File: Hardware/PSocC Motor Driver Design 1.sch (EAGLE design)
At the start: 43 parts, among them J1 DNP, J2 DNP, J3 DNP, J4 DNP, J5 DNP, J6 DNP, J7 DNP, U1 CY8C4245LQI-483, U2 DRV8835

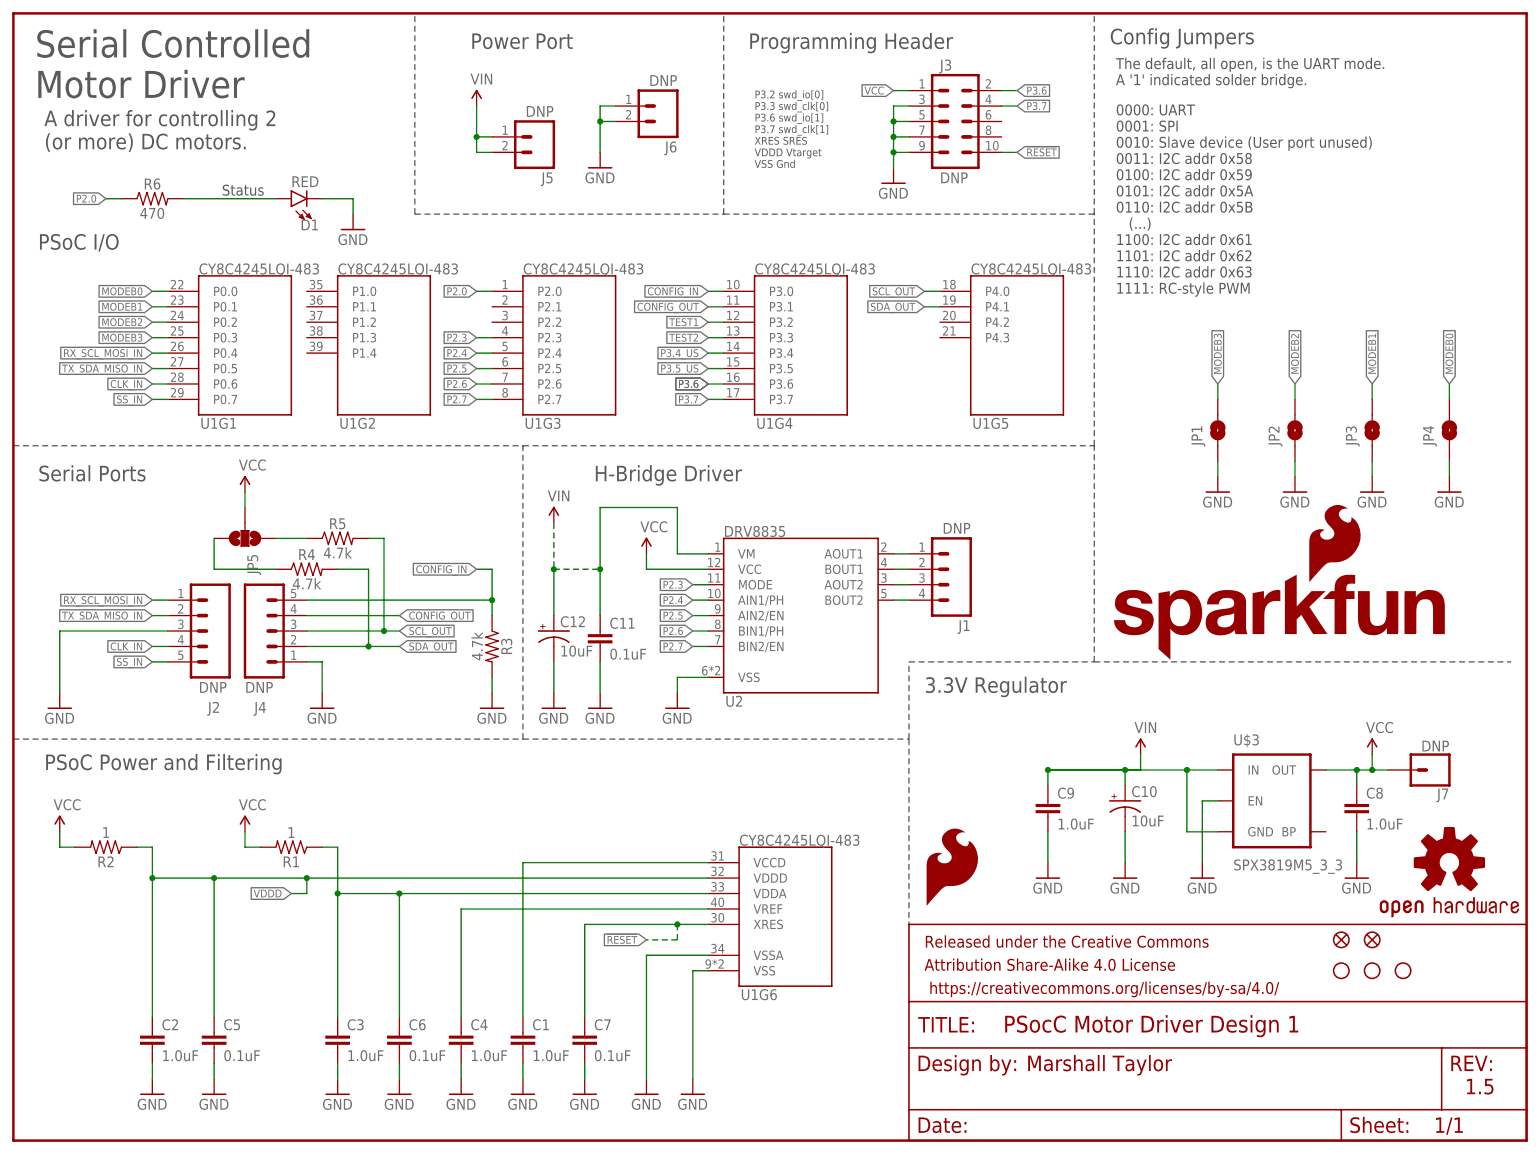
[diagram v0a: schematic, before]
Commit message: Introducing serial psoc project and fixing github issues
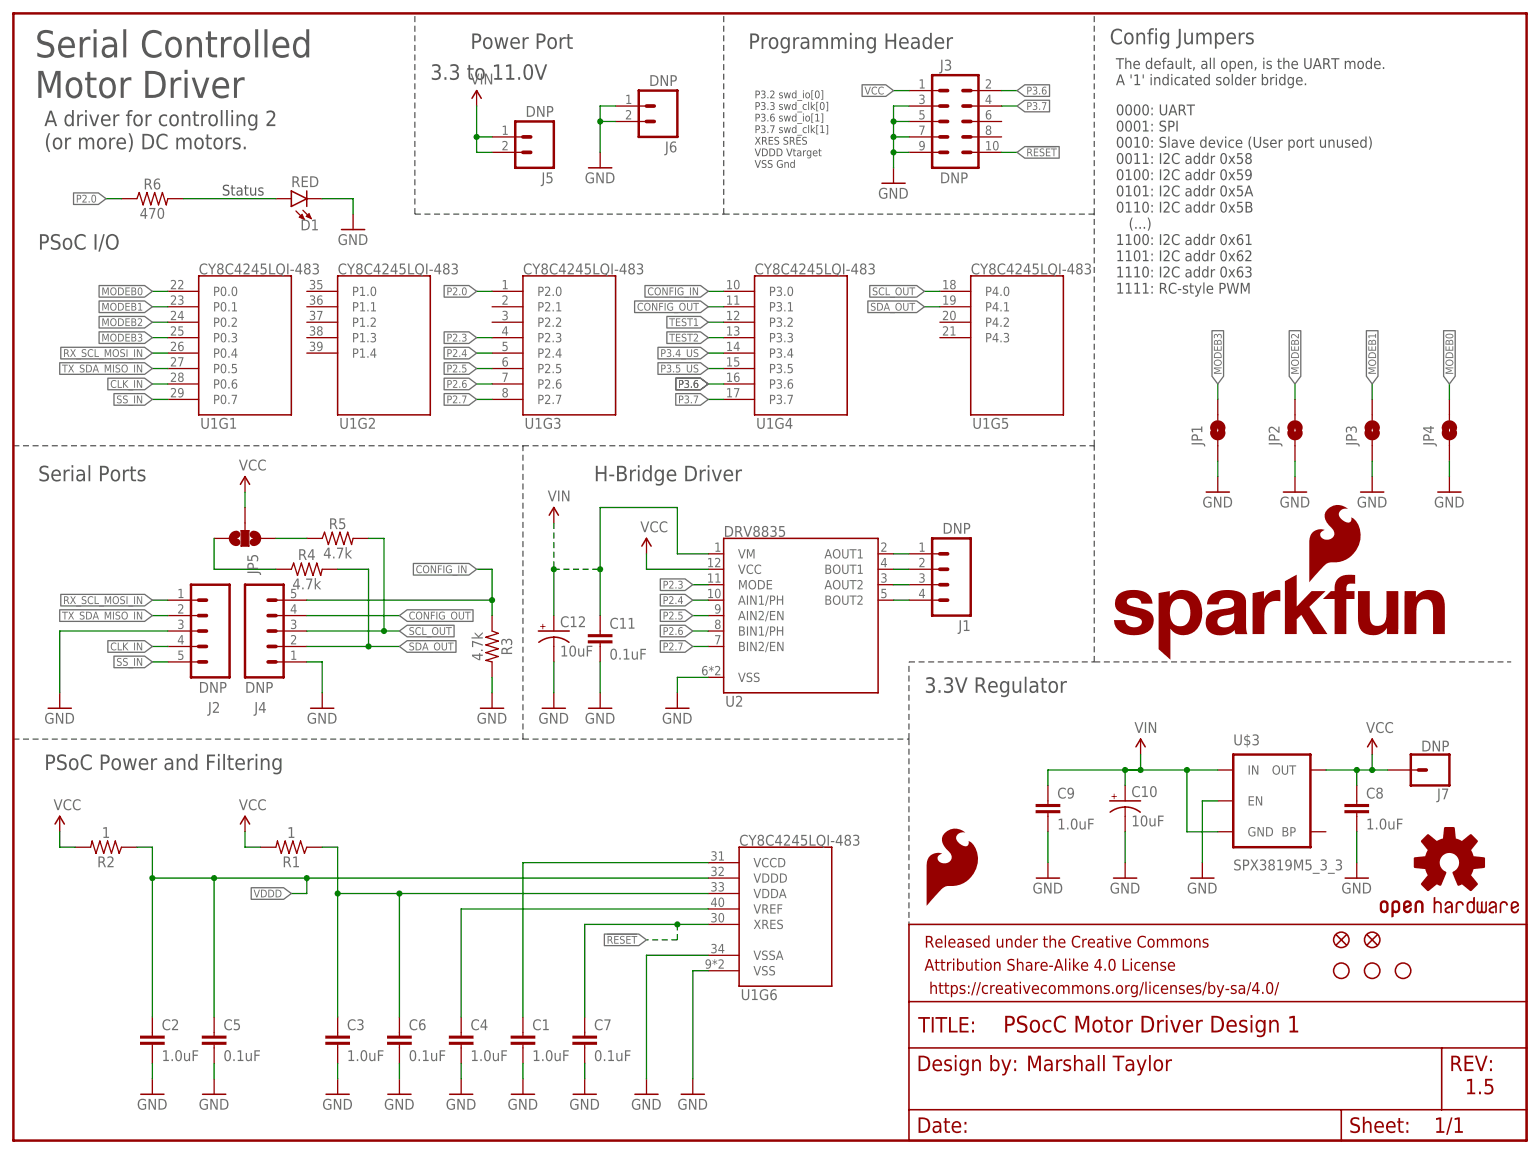
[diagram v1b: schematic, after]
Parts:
- U2: PROD_ID (none) -> IC-13342
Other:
- note added: "3.3 to 11.0V"
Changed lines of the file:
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@@
 <part name="C7" library="SparkFun-Capacitors" deviceset="0.1UF" device="-0402-16V-10%" value="0.1uF"/>
 <part name="GND9" library="SparkFun-Aesthetics" deviceset="GND" device=""/>
-<part name="U2" library="PSOC4TempLib" deviceset="DRV883X" device="" value="DRV8835"/>
+<part name="U2" library="PSOC4TempLib" deviceset="DRV883X" device="" value="DRV8835">
+<attribute name="PROD_ID" value="IC-13342"/>
+</part>
 <part name="J1" library="SparkFun-Connectors" deviceset="M04" device="PTH" value="DNP"/>
 <part name="GND10" library="SparkFun-Aesthetics" deviceset="GND" device=""/>
@@
 A '1' indicated solder bridge.</text>
 <text x="34.29" y="157.226" size="1.778" layer="97" font="vector" align="top-left">Status</text>
+<text x="68.58" y="177.038" size="2.54" layer="97" font="vector" ratio="15" align="top-left">3.3 to 11.0V</text>
 </plain>
 <instances>
@@
 <wire x1="193.04" y1="50.8" x2="193.04" y2="60.96" width="0.1524" layer="91"/>
 <junction x="193.04" y="60.96"/>
-<wire x1="193.04" y1="60.96" x2="182.88" y2="60.96" width="0.1524" layer="91"/>
+<wire x1="193.04" y1="60.96" x2="185.42" y2="60.96" width="0.1524" layer="91"/>
+<wire x1="185.42" y1="60.96" x2="182.88" y2="60.96" width="0.1524" layer="91"/>
 <wire x1="182.88" y1="60.96" x2="170.18" y2="60.96" width="0.1524" layer="91"/>
-<wire x1="170.18" y1="60.96" x2="185.42" y2="60.96" width="0.1524" layer="91"/>
+<wire x1="182.88" y1="60.96" x2="185.42" y2="60.96" width="0.1524" layer="91"/>
 <wire x1="185.42" y1="60.96" x2="185.42" y2="63.5" width="0.1524" layer="91"/>
 <pinref part="SUPPLY10" gate="G$1" pin="VIN"/>
 <pinref part="C9" gate="G$1" pin="1"/>
 <wire x1="170.18" y1="58.42" x2="170.18" y2="60.96" width="0.1524" layer="91"/>
-<junction x="170.18" y="60.96"/>
 <pinref part="U$3" gate="G$1" pin="IN"/>
 <pinref part="U$3" gate="G$1" pin="GND"/>
@@
 <wire x1="182.88" y1="60.96" x2="182.88" y2="58.42" width="0.1524" layer="91"/>
 <junction x="182.88" y="60.96"/>
-</segment>
-<segment>
+<junction x="185.42" y="60.96"/>
+</segment>
+<segment>

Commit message: Updated schematic docu
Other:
- note added: "(3.0 to 11.0V)"
- note removed: "3.3 to 11.0V"
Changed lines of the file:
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@@
 VSS Gnd</text>
 <text x="4.064" y="108.458" size="2.54" layer="97" font="vector" ratio="15">Serial Ports</text>
-<text x="75.184" y="179.578" size="2.54" layer="97" font="vector" ratio="15">Power Port</text>
+<text x="70.104" y="180.594" size="2.54" layer="97" font="vector" ratio="15">Power Port</text>
 <text x="120.904" y="179.578" size="2.54" layer="97" font="vector" ratio="15">Programming Header</text>
 <text x="95.504" y="108.458" size="2.54" layer="97" font="vector" ratio="15">H-Bridge Driver</text>
@@
 A '1' indicated solder bridge.</text>
 <text x="34.29" y="157.226" size="1.778" layer="97" font="vector" align="top-left">Status</text>
-<text x="68.58" y="177.038" size="2.54" layer="97" font="vector" ratio="15" align="top-left">3.3 to 11.0V</text>
+<text x="71.12" y="177.038" size="1.778" layer="97" font="vector" ratio="15">(3.0 to 11.0V)</text>
 </plain>
 <instances>
